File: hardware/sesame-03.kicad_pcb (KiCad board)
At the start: 2 copper layers, 10 parts, among them IC1 ATMEGA8-P, U1 HC-06

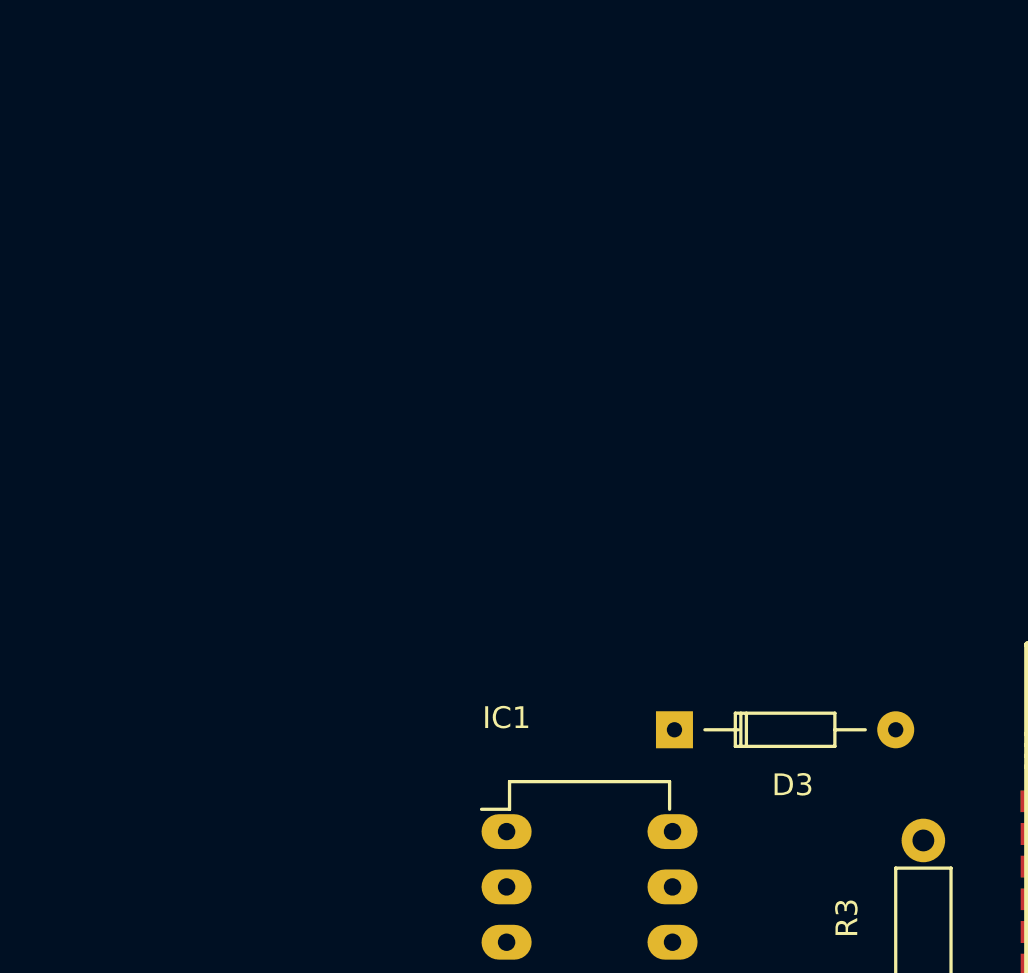
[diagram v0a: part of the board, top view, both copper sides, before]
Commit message: Add kikad files,
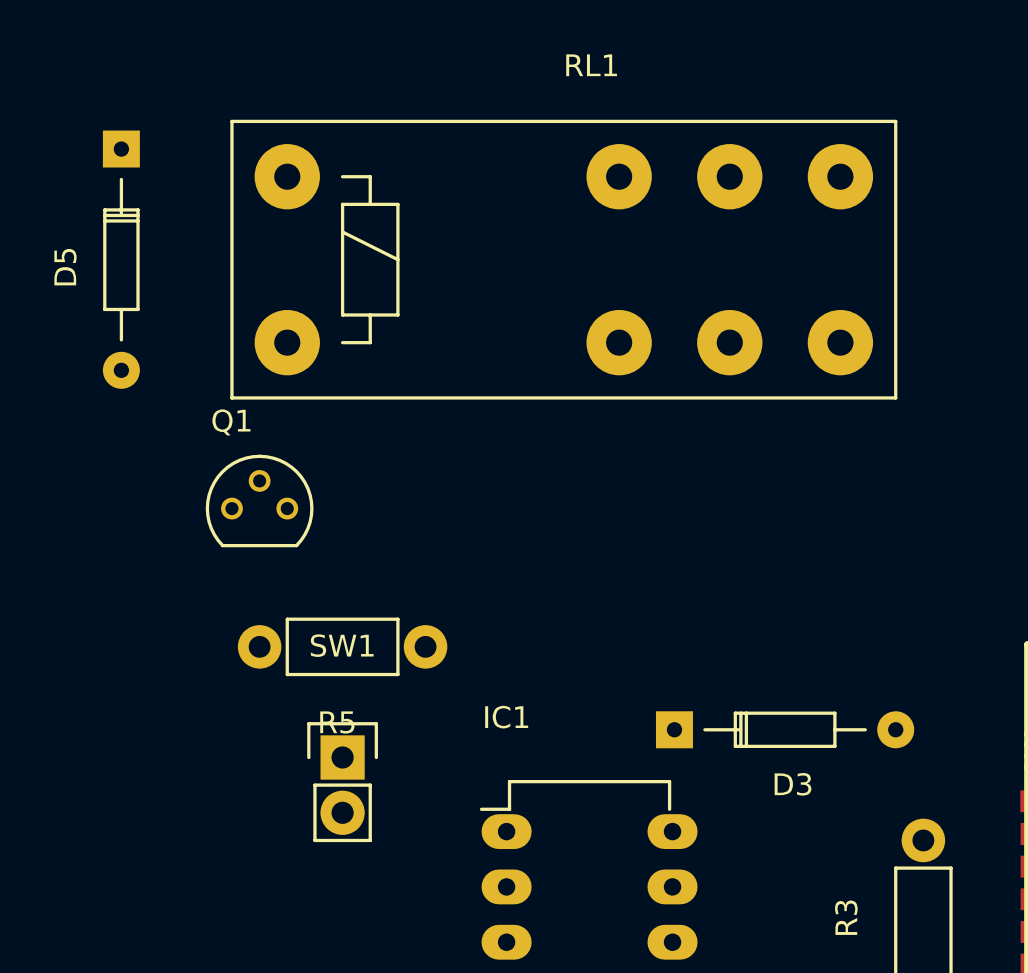
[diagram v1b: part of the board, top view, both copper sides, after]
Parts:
- added D5: 1N4148, Diodes_ThroughHole:Diode_DO-35_SOD27_Horizontal_RM10, F.Cu at (130.8, 73.7)
- added Q1: PN2222A, TO_SOT_Packages_THT:TO-92_Molded_Narrow, F.Cu at (135.9, 90.2)
- added R5: 3K3, Resistors_ThroughHole:Resistor_Horizontal_RM7mm, F.Cu at (144.8, 96.5)
- added RL1: RM50-xx11, Relays_ThroughHole:Relay_SPDT_Schrack-RT1_RM5mm, F.Cu at (138.4, 82.5)
- added SW1: SW_PUSH_SMALL_H, Pin_Headers:Pin_Header_Straight_1x02, F.Cu at (141.0, 101.6)
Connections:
- IC1 pad 1: (no net) -> Net-(IC1-Pad1)
- IC1 pad 28: (no net) -> Net-(IC1-Pad28)
- R3 pad 1: (no net) -> +3V3
- U1 pad 12: (no net) -> +3V3
